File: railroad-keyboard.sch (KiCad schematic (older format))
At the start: 208 parts, among them SW1 SW_Push, U1 ATmega32U4-AU, Y1 16MHz

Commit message: Completion of first draft
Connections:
- net COL0: now also U1.8 (PB0); no longer U1.18 (PD0)
- net COL1: now also U1.9 (PB1); no longer U1.19 (PD1)
- net COL10: now also U1.25 (PD4); no longer U1.39 (PF4)
- net COL2: now also U1.10 (PB2); no longer U1.20 (PD2)
- net COL3: now also U1.11 (PB3); no longer U1.21 (PD3)
- net COL4: now also U1.12 (PB7); no longer U1.25 (PD4)
- net COL5: now also U1.18 (PD0); no longer U1.22 (PD5)
- net COL6: now also U1.19 (PD1); no longer U1.26 (PD6)
- net COL7: now also U1.20 (PD2); no longer U1.27 (PD7)
- net COL8: now also U1.21 (PD3); no longer U1.41 (PF0)
- net COL9: now also U1.22 (PD5); no longer U1.40 (PF1)
- net ROW0: now also U1.26 (PD6); no longer U1.8 (PB0)
- net ROW1: now also U1.27 (PD7); no longer U1.9 (PB1)
- net ROW2: now also U1.28 (PB4); no longer U1.10 (PB2)
- net ROW3: now also U1.29 (PB5); no longer U1.11 (PB3)
- net ROW4: now also U1.31 (PC6); no longer U1.28 (PB4)
- net ROW5: now also U1.30 (PB6); no longer U1.29 (PB5)
- net ROW6: now also U1.40 (PF1); no longer U1.30 (PB6)
- net ROW7: now also U1.41 (PF0); no longer U1.12 (PB7)
- net ROW8: now also U1.32 (PC7); no longer U1.31 (PC6)
- net ROW9: now also U1.39 (PF4); no longer U1.32 (PC7)
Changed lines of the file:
@@
 Wire Wire Line
 	17000 4350 17000 7350
-Text GLabel 2850 12200 2    50   Input ~ 0
+Text GLabel 2850 14000 2    50   Input ~ 0
 ROW1
-Text GLabel 2850 12100 2    50   Input ~ 0
+Text GLabel 2850 13900 2    50   Input ~ 0
 ROW0
-Text GLabel 2850 12400 2    50   Input ~ 0
+Text GLabel 2850 12600 2    50   Input ~ 0
 ROW3
-Text GLabel 2850 12300 2    50   Input ~ 0
+Text GLabel 2850 12500 2    50   Input ~ 0
 ROW2
-Text GLabel 2850 12600 2    50   Input ~ 0
+Text GLabel 2850 12700 2    50   Input ~ 0
 ROW5
-Text GLabel 2850 12500 2    50   Input ~ 0
+Text GLabel 2850 13000 2    50   Input ~ 0
 ROW4
-Text GLabel 2850 12800 2    50   Input ~ 0
+Text GLabel 2850 14500 2    50   Input ~ 0
 ROW7
-Text GLabel 2850 12700 2    50   Input ~ 0
+Text GLabel 2850 14600 2    50   Input ~ 0
 ROW6
+Text GLabel 2850 14700 2    50   Input ~ 0
+ROW9
 Text GLabel 2850 13100 2    50   Input ~ 0
-ROW9
-Text GLabel 2850 13000 2    50   Input ~ 0
 ROW8
 Wire Wire Line
@@
 Wire Wire Line
 	2850 12200 2750 12200
+Text GLabel 2850 12100 2    50   Input ~ 0
+COL0
+Text GLabel 2850 12200 2    50   Input ~ 0
+COL1
+Text GLabel 2850 12300 2    50   Input ~ 0
+COL2
+Text GLabel 2850 12400 2    50   Input ~ 0
+COL3
+Text GLabel 2850 12800 2    50   Input ~ 0
+COL4
 Text GLabel 2850 13300 2    50   Input ~ 0
-COL0
+COL5
+Text GLabel 2850 13500 2    50   Input ~ 0
+COL7
+Text GLabel 2850 13600 2    50   Input ~ 0
+COL8
+Text GLabel 2850 13800 2    50   Input ~ 0
+COL9
+Text GLabel 2850 13700 2    50   Input ~ 0
+COL10
 Text GLabel 2850 13400 2    50   Input ~ 0
-COL1
-Text GLabel 2850 13500 2    50   Input ~ 0
-COL2
-Text GLabel 2850 13600 2    50   Input ~ 0
-COL3
-Text GLabel 2850 13700 2    50   Input ~ 0
-COL4
-Text GLabel 2850 13800 2    50   Input ~ 0
-COL5
-Text GLabel 2850 14000 2    50   Input ~ 0
-COL7
-Text GLabel 2850 14500 2    50   Input ~ 0
-COL8
-Text GLabel 2850 14600 2    50   Input ~ 0
-COL9
-Text GLabel 2850 14700 2    50   Input ~ 0
-COL10
-Text GLabel 2850 13900 2    50   Input ~ 0
 COL6
 Wire Wire Line

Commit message: Major revisions to schema
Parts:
- removed USB1: Molex-0548190589, random-keyboard-parts:Molex-0548190589, symbol random-keyboard-parts:Molex-0548190589
- added C8: 4.7uF, Capacitor_SMD:C_0805_2012Metric, symbol Device:C_Small
- added J1: 1734510-1, TE_1734510-1, symbol 1734510-1:1734510-1
- added R5: 1m, Resistor_SMD:R_0805_2012Metric, symbol Device:R_Small
- added R6: 10k, Resistor_SMD:R_0805_2012Metric, symbol Device:R_Small
- added R7, R8: 4.7k, Resistor_SMD:R_0805_2012Metric, symbol Device:R_Small
- added U2: TRRS, Keebio-Parts:TRRS-PJ-320A, symbol keebio:TRRS
- C1, C2, C3, C5, C6, C7: footprint Diode_SMD:D_SOD-123 -> Capacitor_SMD:C_0805_2012Metric
- C4: value 10uF -> 4.7uF; footprint Diode_SMD:D_SOD-123 -> Capacitor_SMD:C_0805_2012Metric
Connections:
- net +5V: now also R7.1, R8.1, U2.1 (SLEEVE)
- net COL10: now also U1.30 (PB6); no longer U1.25 (PD4)
- net COL5: now also U1.25 (PD4); no longer U1.18 (PD0)
- net COL6: now also U1.26 (PD6); no longer U1.19 (PD1)
- net COL7: now also U1.27 (PD7); no longer U1.20 (PD2)
- net COL8: now also U1.28 (PB4); no longer U1.21 (PD3)
- net COL9: now also U1.29 (PB5); no longer U1.22 (PD5)
- net D+: now also J1.3 (D+)
- net D-: now also J1.2 (D-)
- net GND: now also C8.1, J1.5 (GND), R6.1, U2.2 (TIP)
- net ROW0: now also U1.20 (PD2); no longer U1.26 (PD6)
- net ROW1: now also U1.21 (PD3); no longer U1.27 (PD7)
- net ROW2: now also U1.22 (PD5); no longer U1.28 (PB4)
- net ROW3: now also U1.31 (PC6); no longer U1.29 (PB5)
- net ROW4: now also U1.32 (PC7); no longer U1.31 (PC6)
- net ROW5: now also U1.37 (PF6); no longer U1.30 (PB6)
- net ROW6: now also U1.38 (PF5); no longer U1.40 (PF1)
- net ROW7: now also U1.39 (PF4); no longer U1.41 (PF0)
- net ROW8: now also U1.40 (PF1); no longer U1.32 (PC7)
- net ROW9: now also U1.41 (PF0); no longer U1.39 (PF4)
- net VCC: now also J1.1 (VCC)
- net at U1.36 (PF7): now also R6.2
- new net: J1.SH1 (SHIELD), J1.SH2 (SHIELD), R5.1
- new net: C8.2, R5.2
- new net LHD0: R7.2, U1.18 (PD0), U2.4 (RING2)
- new net LHD1: R8.2, U1.19 (PD1), U2.3 (RING1)
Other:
- moved on the sheet: F1

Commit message: Further major revisions
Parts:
- J1: footprint TE_1734510-1 -> usb-mini-1734510-1:TE_1734510-1
- MX0, MX1, MX10, MX101, MX102, MX103, MX104, MX105, MX106, MX107, MX108, MX109, MX2, MX200, MX202, MX203, MX204, MX205, MX206, MX207, MX208, MX3, MX301, MX302, MX303, MX304, MX305, MX306, MX307, MX308, MX309, MX4, MX402, MX403, MX404, MX405, MX406, MX407, MX408, MX409, MX5, MX501, MX502, MX503, MX504, MX505, MX506, MX507, MX508, MX6, MX600, MX602, MX603, MX604, MX605, MX606, MX607, MX608, MX7, MX701, MX702, MX703, MX704, MX705, MX706, MX707, MX708, MX709, MX8, MX800, MX809, MX810, MX900, MX902, MX907, MX909: footprint MX_Alps_Hybrid:MX-1U-NoLED -> MX_Only:MXOnly-1U-NoLED
- MX100, MX9: footprint MX_Alps_Hybrid:MX-2U-NoLED -> MX_Only:MXOnly-2U-NoLED
- MX201, MX209, MX300, MX801, MX808, MX908: footprint MX_Alps_Hybrid:MX-1.5U-NoLED -> MX_Only:MXOnly-1.5U-NoLED
- MX400, MX802, MX901: footprint MX_Alps_Hybrid:MX-1.25U-NoLED -> MX_Only:MXOnly-1.25U-NoLED
- MX401, MX905: footprint MX_Alps_Hybrid:MX-2.25U-NoLED -> MX_Only:MXOnly-2.25U-NoLED
- MX410: footprint MX_Alps_Hybrid:MX-ISO -> MX_Only:MXOnly-ISO-ROTATED-ReversedStabilizers-NoLED
- MX509, MX609, MX903, MX906: footprint MX_Alps_Hybrid:MX-1.75U-NoLED -> MX_Only:MXOnly-1.75U-NoLED
- MX601, MX904: footprint MX_Alps_Hybrid:MX-2.75U-NoLED -> MX_Only:MXOnly-2.75U-NoLED
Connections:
- net GND: now also R5.2
- net at J1.SH1 (SHIELD), J1.SH2 (SHIELD), R5.1: now also C8.2
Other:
- moved on the sheet: C8, R5

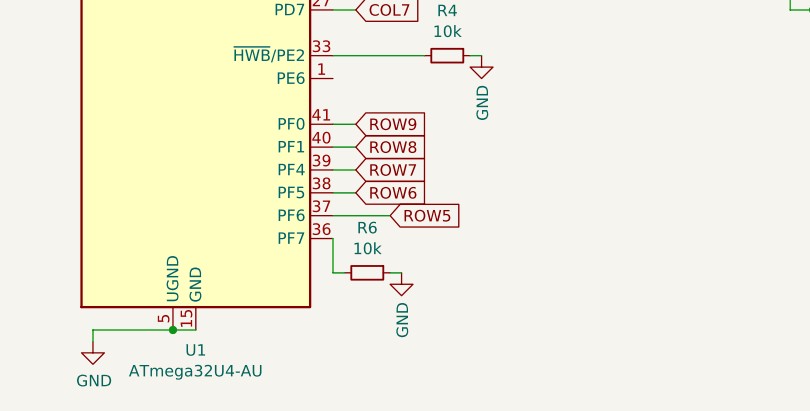
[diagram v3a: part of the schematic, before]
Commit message: Start reworking routing again
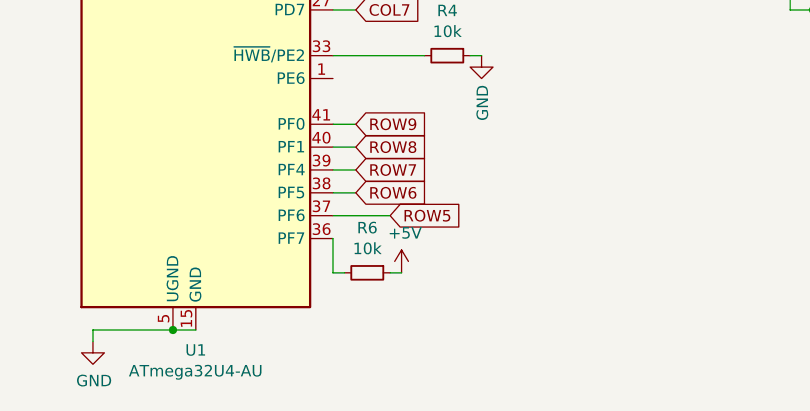
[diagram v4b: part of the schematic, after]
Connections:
- net +5V: now also R6.1
- net GND: no longer R6.1
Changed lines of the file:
@@
 	3050 15150 3000 15150
-$Comp
-L power:GND #PWR0114
-U 1 1 5F41B2E6
-P 3050 15150
-F 0 "#PWR0114" H 3050 14900 50  0001 C CNN
-F 1 "GND" V 3055 15022 50  0000 R CNN
-F 2 "" H 3050 15150 50  0001 C CNN
-F 3 "" H 3050 15150 50  0001 C CNN
-	1    3050 15150
-	1    0    0    -1
-$EndComp
 $Comp
 L Device:R_Small R6
@@
 Wire Wire Line
 	5100 13100 5350 13100
+$Comp
+L power:+5V #PWR?
+U 1 1 5F06495B
+P 3050 15150
+F 0 "#PWR?" H 3050 15000 50  0001 C CNN
+F 1 "+5V" H 3065 15323 50  0000 C CNN
+F 2 "" H 3050 15150 50  0001 C CNN
+F 3 "" H 3050 15150 50  0001 C CNN
+	1    3050 15150
+	1    0    0    -1
+$EndComp
 $EndSCHEMATC

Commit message: Backup prior to adding silkscreen
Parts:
- added D500: SOD-123, Diode_SMD:D_SOD-123, symbol Device:D_Small
- added MX100_alt1, MX500_alt2: MX-NoLED, MX_Only:MXOnly-1U-NoLED, symbol MX_Alps_Hybrid:MX-NoLED
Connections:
- net +5V: no longer R7.1, R8.1, U2.1 (SLEEVE)
- net COL0: now also MX100_alt1.1 (COL), MX500_alt2.1 (COL)
- net ROW5: now also D500.1 (K)
- net VCC: now also R7.1, R8.1, U2.1 (SLEEVE)
- net at D100.2 (A), MX100.2 (ROW): now also MX100_alt1.2 (ROW)
- new net: D500.2 (A), MX500_alt2.2 (ROW)
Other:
- moved on the sheet: D100
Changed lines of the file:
@@
 L Device:D_Small D100
 U 1 1 5EFD4486
-P 2300 1400
-F 0 "D100" H 2250 1500 50  0000 C CNN
-F 1 "SOD-123" H 2750 1500 50  0000 R CNN
-F 2 "Diode_SMD:D_SOD-123" V 2300 1400 50  0001 C CNN
-F 3 "~" V 2300 1400 50  0001 C CNN
-	1    2300 1400
+P 2300 1500
+F 0 "D100" H 2250 1600 50  0000 C CNN
+F 1 "SOD-123" H 2750 1600 50  0000 R CNN
+F 2 "Diode_SMD:D_SOD-123" V 2300 1500 50  0001 C CNN
+F 3 "~" V 2300 1500 50  0001 C CNN
+	1    2300 1500
 	0    -1   -1   0
 $EndComp
@@
 Connection ~ 15300 1750
 Wire Wire Line
-	2300 1500 2300 2000
-Wire Wire Line
-	2300 2000 1000 2000
-Wire Wire Line
-	2300 2000 3800 2000
-Wire Wire Line
 	3800 2000 3800 1500
-Connection ~ 2300 2000
 Wire Wire Line
 	3800 2000 5300 2000
@@
 Connection ~ 14300 8250
 Wire Wire Line
-	1000 5250 3800 5250
+	1000 5250 2300 5250
 Wire Wire Line
 	1000 6750 3800 6750
@@
 	4800 8000 13800 8000
 Wire Wire Line
-	2500 7350 2500 2850
+	2500 7350 2500 4350
 Connection ~ 2500 1100
 Wire Wire Line
@@
 LHD1
 $Comp
-L power:+5V #PWR0115
-U 1 1 5F586918
-P 5150 11750
-F 0 "#PWR0115" H 5150 11600 50  0001 C CNN
-F 1 "+5V" H 5165 11923 50  0000 C CNN
-F 2 "" H 5150 11750 50  0001 C CNN
-F 3 "" H 5150 11750 50  0001 C CNN
-	1    5150 11750
-	1    0    0    -1
-$EndComp
-$Comp
 L power:GND #PWR0116
 U 1 1 5F5889FE
@@
 	5100 13100 5350 13100
 $Comp
-L power:+5V #PWR?
+L power:+5V #PWR0114
 U 1 1 5F06495B
 P 3050 15150
-F 0 "#PWR?" H 3050 15000 50  0001 C CNN
+F 0 "#PWR0114" H 3050 15000 50  0001 C CNN
 F 1 "+5V" H 3065 15323 50  0000 C CNN
 F 2 "" H 3050 15150 50  0001 C CNN
@@
 	1    0    0    -1
 $EndComp
+$Comp
+L power:VCC #PWR0115
+U 1 1 5F08F143
+P 5150 11750
+F 0 "#PWR0115" H 5150 11600 50  0001 C CNN
+F 1 "VCC" H 5165 11923 50  0000 C CNN
+F 2 "" H 5150 11750 50  0001 C CNN
+F 3 "" H 5150 11750 50  0001 C CNN
+	1    5150 11750
+	1    0    0    -1
+$EndComp
+$Comp
+L MX_Alps_Hybrid:MX-NoLED MX100_alt1
+U 1 1 5F09C085
+P 2700 1150
+F 0 "MX100_alt1" H 2733 1373 60  0000 C CNN
+F 1 "MX-NoLED" H 2733 1299 20  0000 C CNN
+F 2 "MX_Only:MXOnly-1U-NoLED" H 2075 1125 60  0001 C CNN
+F 3 "" H 2075 1125 60  0001 C CNN
+	1    2700 1150
+	1    0    0    -1
+$EndComp
+Wire Wire Line
+	1000 2000 2300 2000
+Wire Wire Line
+	2850 850  2850 1100
+Wire Wire Line
+	2500 850  2850 850
+Wire Wire Line
+	2650 1300 2300 1300
+Wire Wire Line
+	2300 1300 2300 1400
+Connection ~ 2300 1300
+$Comp
+L MX_Alps_Hybrid:MX-NoLED MX500_alt2
+U 1 1 5F18449D
+P 2350 4400
+F 0 "MX500_alt2" H 2383 4623 60  0000 C CNN
+F 1 "MX-NoLED" H 2383 4549 20  0000 C CNN
+F 2 "MX_Only:MXOnly-1U-NoLED" H 1725 4375 60  0001 C CNN
+F 3 "" H 1725 4375 60  0001 C CNN
+	1    2350 4400
+	1    0    0    -1
+$EndComp
+Connection ~ 2500 4350
+Wire Wire Line
+	2500 4350 2500 2850
+$Comp
+L Device:D_Small D500
+U 1 1 5F1B210F
+P 2300 4650
+F 0 "D500" H 2250 4750 50  0000 C CNN
+F 1 "SOD-123" H 2750 4750 50  0000 R CNN
+F 2 "Diode_SMD:D_SOD-123" V 2300 4650 50  0001 C CNN
+F 3 "~" V 2300 4650 50  0001 C CNN
+	1    2300 4650
+	0    -1   -1   0
+$EndComp
+Wire Wire Line
+	2300 4750 2300 5250
+Connection ~ 2300 5250
+Wire Wire Line
+	2300 5250 3800 5250
+Wire Wire Line
+	2300 1600 2300 2000
+Connection ~ 2300 2000
+Wire Wire Line
+	2300 2000 3800 2000
 $EndSCHEMATC

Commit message: Just about ready to send to JLCPCB
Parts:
- added J2, J3: Conn_01x01, Connector_PinHeader_1.00mm:PinHeader_1x01_P1.00mm_Horizontal, symbol Connector_Generic:Conn_01x01
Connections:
- new net GND1: J2.1 (Pin_1)
- new net GND2: J3.1 (Pin_1)
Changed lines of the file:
@@
 Wire Wire Line
 	2300 2000 3800 2000
+$Comp
+L power:GND1 #PWR0118
+U 1 1 5F0E4864
+P 6900 13000
+F 0 "#PWR0118" H 6900 12750 50  0001 C CNN
+F 1 "GND1" H 6905 12827 50  0000 C CNN
+F 2 "" H 6900 13000 50  0001 C CNN
+F 3 "" H 6900 13000 50  0001 C CNN
+	1    6900 13000
+	1    0    0    -1
+$EndComp
+$Comp
+L power:GND2 #PWR0119
+U 1 1 5F145BBF
+P 6850 13700
+F 0 "#PWR0119" H 6850 13450 50  0001 C CNN
+F 1 "GND2" H 6855 13527 50  0000 C CNN
+F 2 "" H 6850 13700 50  0001 C CNN
+F 3 "" H 6850 13700 50  0001 C CNN
+	1    6850 13700
+	1    0    0    -1
+$EndComp
+$Comp
+L Connector_Generic:Conn_01x01 J2
+U 1 1 5F2DF526
+P 7100 13000
+F 0 "J2" H 7180 13042 50  0000 L CNN
+F 1 "Conn_01x01" H 7180 12951 50  0000 L CNN
+F 2 "Connector_PinHeader_1.00mm:PinHeader_1x01_P1.00mm_Horizontal" H 7100 13000 50  0001 C CNN
+F 3 "~" H 7100 13000 50  0001 C CNN
+	1    7100 13000
+	1    0    0    -1
+$EndComp
+$Comp
+L Connector_Generic:Conn_01x01 J3
+U 1 1 5F3408A6
+P 7050 13700
+F 0 "J3" H 7130 13742 50  0000 L CNN
+F 1 "Conn_01x01" H 7130 13651 50  0000 L CNN
+F 2 "Connector_PinHeader_1.00mm:PinHeader_1x01_P1.00mm_Horizontal" H 7050 13700 50  0001 C CNN
+F 3 "~" H 7050 13700 50  0001 C CNN
+	1    7050 13700
+	1    0    0    -1
+$EndComp
 $EndSCHEMATC

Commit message: Update Reset Switch and routing
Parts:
- SW1: footprint random-keyboard-parts:SKQG-1155865 -> Keebio-Parts:SW_Tactile_SPST_Angled_MJTP1117
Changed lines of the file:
@@
 F 0 "SW1" H 1250 12135 50  0000 C CNN
 F 1 "SW_Push" H 1250 12044 50  0000 C CNN
-F 2 "random-keyboard-parts:SKQG-1155865" H 1250 12050 50  0001 C CNN
+F 2 "Keebio-Parts:SW_Tactile_SPST_Angled_MJTP1117" H 1250 12050 50  0001 C CNN
 F 3 "~" H 1250 12050 50  0001 C CNN
 	1    1250 11850

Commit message: Update for new machine
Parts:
- C1, C2, C3, C4, C5, C6, C7, C8: symbol Device:C_Small -> railroad-keyboard-rescue:C_Small-Device
- D0, D1, D10, D100, D101, D102, D103, D104, D105, D106, D107, D108, D109, D2, D200, D201, D202, D203, D204, D205, D206, D207, D208, D209, D3, D300, D301, D302, D303, D304, D305, D306, D307, D308, D309, D4, D400, D401, D402, D403, D404, D405, D406, D407, D408, D409, D410, D5, D500, D501, D502, D503, D504, D505, D506, D507, D508, D509, D6, D600, D601, D602, D603, D604, D605, D606, D607, D608, D609, D7, D701, D702, D703, D704, D705, D706, D707, D708, D709, D8, D800, D801, D802, D808, D809, D810, D9, D900, D901, D902, D903, D904, D905, D906, D907, D908, D909: symbol Device:D_Small -> railroad-keyboard-rescue:D_Small-Device
- F1: symbol Device:Polyfuse -> railroad-keyboard-rescue:Polyfuse-Device
- J1: symbol 1734510-1:1734510-1 -> railroad-keyboard-rescue:1734510-1-1734510-1
- J2, J3: symbol Connector_Generic:Conn_01x01 -> railroad-keyboard-rescue:Conn_01x01-Connector_Generic
- MX0, MX1, MX10, MX100, MX100_alt1, MX101, MX102, MX103, MX104, MX105, MX106, MX107, MX108, MX109, MX2, MX200, MX201, MX202, MX203, MX204, MX205, MX206, MX207, MX208, MX209, MX3, MX300, MX301, MX302, MX303, MX304, MX305, MX306, MX307, MX308, MX309, MX4, MX400, MX401, MX402, MX403, MX404, MX405, MX406, MX407, MX408, MX409, MX410, MX5, MX500_alt2, MX501, MX502, MX503, MX504, MX505, MX506, MX507, MX508, MX509, MX6, MX600, MX601, MX602, MX603, MX604, MX605, MX606, MX607, MX608, MX609, MX7, MX701, MX702, MX703, MX704, MX705, MX706, MX707, MX708, MX709, MX8, MX800, MX801, MX802, MX808, MX809, MX810, MX9, MX900, MX901, MX902, MX903, MX904, MX905, MX906, MX907, MX908, MX909: symbol MX_Alps_Hybrid:MX-NoLED -> railroad-keyboard-rescue:MX-NoLED-MX_Alps_Hybrid
- R1, R2, R3, R4, R5, R6, R7, R8: symbol Device:R_Small -> railroad-keyboard-rescue:R_Small-Device
- SW1: symbol Switch:SW_Push -> railroad-keyboard-rescue:SW_Push-Switch
- U1: symbol MCU_Microchip_ATmega:ATmega32U4-AU -> railroad-keyboard-rescue:ATmega32U4-AU-MCU_Microchip_ATmega
- U2: symbol keebio:TRRS -> railroad-keyboard-rescue:TRRS-keebio
- Y1: symbol Device:Crystal_GND24_Small -> railroad-keyboard-rescue:Crystal_GND24_Small-Device
